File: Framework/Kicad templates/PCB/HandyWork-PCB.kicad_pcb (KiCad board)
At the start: 4 copper layers, 283.2 x 131.5 mm, 53 parts, among them J1 Conn_01x04, J2 Conn_02x04_Odd_Even, SW1 KXT3, SW2 KXT3, U1 RP2040, U2 W25Q16JV, U3 IS31FL3733B-QF, Y1 12.000 MHz

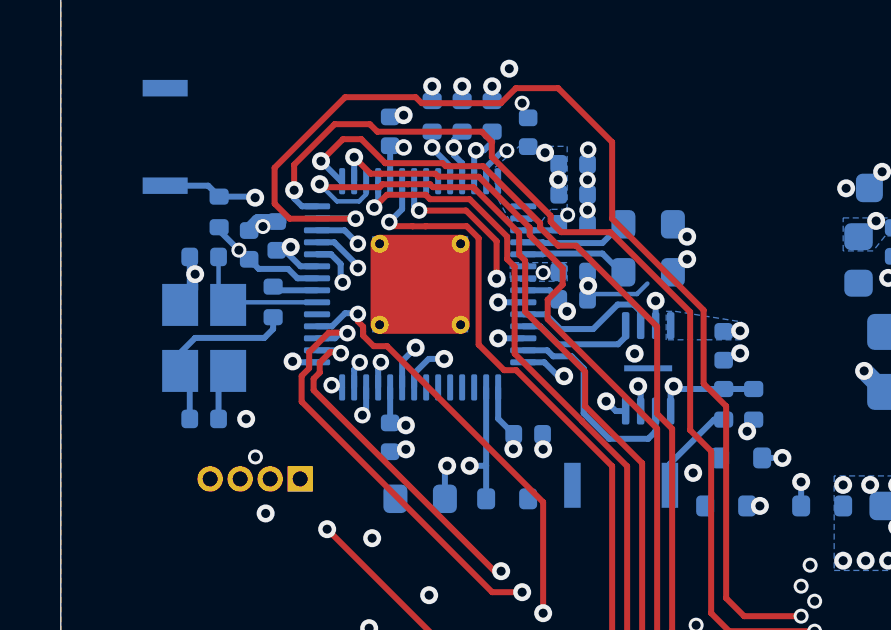
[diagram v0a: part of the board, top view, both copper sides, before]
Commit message: HandyWork (template and 5x3-M-N): Small touches ups, almost ready for prod
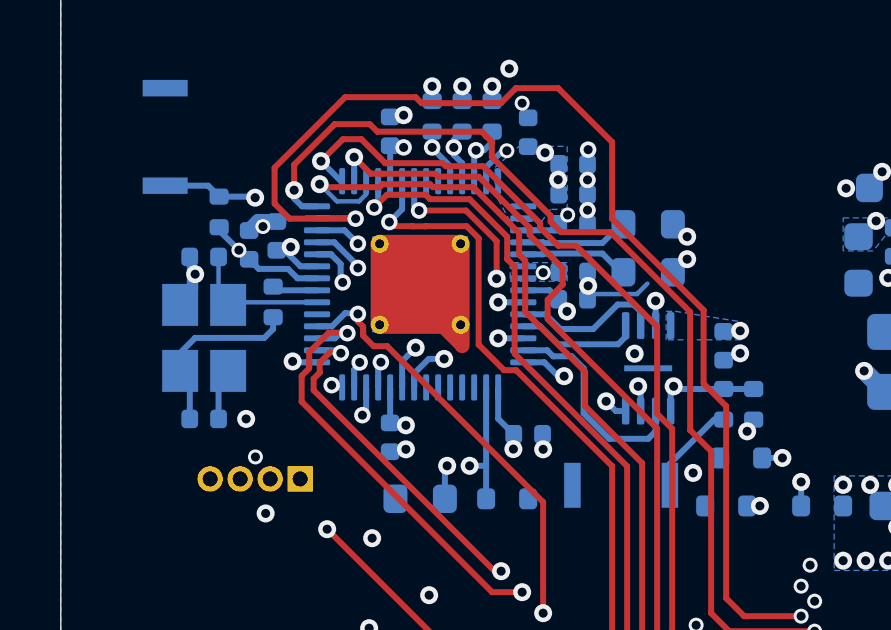
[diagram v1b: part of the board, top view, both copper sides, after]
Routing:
- net GND: track 55.7 -> 59.0 mm
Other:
- board text added: "HW--${REVISION}"
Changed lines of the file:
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@@
 	(title_block
 		(title "HandyWork - PCB Template")
-		(date "2026-03-01")
-		(rev "1.0")
+		(date "2026-03-04")
+		(rev "v1A")
 		(company "Axel Voitier")
 		(comment 1 "HandyWork - PCB Template")
@@
 			(outputformat 1)
 			(mirror no)
-			(drillshape 1)
+			(drillshape 0)
 			(scaleselection 1)
-			(outputdirectory "")
+			(outputdirectory "Fab/")
 		)
 	)
@@
 		(tags "capacitor")
 		(property "Reference" "C5"
-			(at 1.8875 0.2 270)
+			(at 1.8875 0.38 270)
 			(layer "B.SilkS")
 			(effects
@@
 		(tags "capacitor")
 		(property "Reference" "C10"
-			(at -0.6 1.5 180)
+			(at 1.4 -0.9375 180)
 			(layer "B.SilkS")
 			(effects
@@
 		)
 	)
+	(gr_text "HW--${REVISION}"
+		(at 285.5 137 0)
+		(layer "B.SilkS")
+		(effects
+			(font
+				(face "Ubuntu")
+				(size 1 1)
+				(thickness 0.25)
+				(bold yes)
+			)
+			(justify left bottom mirror)
+		)
+		(render_cache "HW--v1A" 0
+			(polygon
+				(pts
+					(xy 284.803297 135.860844) (xy 284.585066 135.860844) (xy 284.585066 136.83) (xy 284.803297 136.83)
+					(xy 284.803297 136.419672) (xy 285.169844 136.419672) (xy 285.169844 136.83) (xy 285.388075 136.83)
+					(xy 285.388075 135.860844) (xy 285.169844 135.860844) (xy 285.169844 136.232093) (xy 284.803297 136.232093)
+				)
+			)
+			(polygon
+				(pts
+					(xy 283.710737 135.962449) (xy 283.673674 136.092203) (xy 283.630321 136.241618) (xy 283.583487 136.395919)
+					(xy 283.537264 136.538984) (xy 283.5002 136.383768) (xy 283.46448 136.210416) (xy 283.431629 136.032119)
+					(xy 283.401526 135.860844) (xy 283.17493 135.860844) (xy 283.227291 136.104661) (xy 283.287587 136.35452)
+					(xy 283.35462 136.601262) (xy 283.42534 136.83) (xy 283.625375 136.83) (xy 283.720568 136.547349)
+					(xy 283.811488 136.250655) (xy 283.901003 136.547349) (xy 283.947287 136.693444) (xy 283.994731 136.83)
+					(xy 284.194827 136.83) (xy 284.265561 136.601265) (xy 284.332641 136.35452) (xy 284.392891 136.104662)
+					(xy 284.445237 135.860844) (xy 284.20881 135.860844) (xy 284.178035 136.032119) (xy 284.143047 136.210416)
+					(xy 284.105983 136.383768) (xy 284.067515 136.538984) (xy 284.018545 136.39311) (xy 283.972383 136.23881)
+					(xy 283.931106 136.090127) (xy 283.896789 135.962449)
+				)
+			)
+			(polygon
+				(pts
+					(xy 283.111488 136.318066) (xy 282.7058 136.318066) (xy 282.7058 136.505645) (xy 283.111488 136.505645)
+				)
+			)
+			(polygon
+				(pts
+					(xy 282.635703 136.318066) (xy 282.230015 136.318066) (xy 282.230015 136.505645) (xy 282.635703 136.505645)
+				)
+			)
+			(polygon
+				(pts
+					(xy 281.896929 136.83) (xy 281.966462 136.683704) (xy 282.041704 136.503203) (xy 282.11199 136.311273)
+					(xy 282.180922 136.095317) (xy 281.959883 136.095317) (xy 281.927032 136.213347) (xy 281.887831 136.341819)
+					(xy 281.847226 136.468215) (xy 281.807353 136.579895) (xy 281.768213 136.468215) (xy 281.726936 136.341819)
+					(xy 281.687796 136.213347) (xy 281.654884 136.095317) (xy 281.439462 136.095317) (xy 281.508395 136.311273)
+					(xy 281.578681 136.503203) (xy 281.653922 136.683704) (xy 281.723456 136.83)
+				)
+			)
+			(polygon
+				(pts
+					(xy 281.32711 136.064054) (xy 281.24248 136.02528) (xy 281.156446 135.977287) (xy 281.075968 135.922271)
+					(xy 281.039111 135.892166) (xy 281.006725 135.860844) (xy 280.861217 135.860844) (xy 280.861217 136.83)
+					(xy 281.069678 136.83) (xy 281.069678 136.134396) (xy 281.113375 136.160467) (xy 281.163407 136.184893)
+					(xy 281.264157 136.224277)
+				)
+			)
+			(polygon
+				(pts
+					(xy 280.325104 136.067107) (xy 280.417428 136.290162) (xy 280.513232 136.540511) (xy 280.616791 136.83)
+					(xy 280.390134 136.83) (xy 280.355879 136.726929) (xy 280.318815 136.618974) (xy 279.941032 136.618974)
+					(xy 279.90403 136.727051) (xy 279.869713 136.83) (xy 279.636095 136.83) (xy 279.739593 136.540511)
+					(xy 279.77539 136.447027) (xy 279.992812 136.447027) (xy 280.26844 136.447027) (xy 280.224354 136.32692)
+					(xy 280.184481 136.222201) (xy 280.152302 136.137876) (xy 280.131297 136.080479) (xy 280.108949 136.138243)
+					(xy 280.076099 136.222445) (xy 280.036226 136.327103) (xy 279.992812 136.447027) (xy 279.77539 136.447027)
+					(xy 279.835458 136.290162) (xy 279.928454 136.067107) (xy 280.022182 135.860844) (xy 280.230643 135.860844)
+				)
+			)
+		)
+	)
 	(gr_text "PCB Template"
 		(at 285.5 135 0)
@@
 		(net 1)
 	)
+	(segment
+		(start 20.3 139.7875)
+		(end 20.3 140.483635)
+		(width 0.5)
+		(layer "F.Cu")
+		(net 2)
+	)
+	(segment
+		(start 18.9 139.133635)
+		(end 18.9 138.4375)
+		(width 0.5)
+		(layer "F.Cu")
+		(net 2)
+	)
+	(segment
+		(start 20.25 140.483635)
+		(end 18.9 139.133635)
+		(width 0.4)
+		(layer "F.Cu")
+		(net 2)
+	)
 	(via

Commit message: HandyWork: Harmonise a few things, and add bind points with alu plates
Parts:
- added TP1: TestPoint, TestPoint:TestPoint_THTPad_2.5x2.5mm_Drill1.2mm, B.Cu at (13.5, 45.0)
- added TP2: TestPoint, TestPoint:TestPoint_THTPad_2.5x2.5mm_Drill1.2mm, B.Cu at (148.5, 45.0)
- added TP3: TestPoint, TestPoint:TestPoint_THTPad_2.5x2.5mm_Drill1.2mm, B.Cu at (283.5, 45.0)
- added TP4: TestPoint, TestPoint:TestPoint_THTPad_2.5x2.5mm_Drill1.2mm, B.Cu at (148.5, 140.0)
- added TP5: TestPoint, TestPoint:TestPoint_THTPad_2.5x2.5mm_Drill1.2mm, B.Cu at (283.5, 150.0)
- added TP6: TestPoint, TestPoint:TestPoint_THTPad_2.5x2.5mm_Drill1.2mm, B.Cu at (13.5, 152.5)
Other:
- board text added: "${COMMENT1}-${REVISION}"
- board text added: "${COMMENT4}"
- board text added: "${COMMENT5}"
- board text removed: "HW--${REVISION}"
- board text removed: "HandyWork"
- board text removed: "PCB Template"
